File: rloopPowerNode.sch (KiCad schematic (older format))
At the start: 93 parts, among them P1 CONN_01X02, P10 CONN_01X03, P11 CONN_01X03, P13 CONN_01X03, P14 CONN_01X03, P15 CONN_01X01, P16 CONN_01X01, P17 CONN_01X08, P18 CONN_01X02, P19 CONN_01X02, P2 CONN_01X02, P20 CONN_01X02, P21 CONN_01X02, P22 AMPMODU-02X05, P23 SHUNT, P3 CONN_01X02, P4 CONN_01X02, P5 CONN_01X01, P6 CONN_01X04, P7 CONN_01X02, P8 CONN_01X02, P9 CONN_01X02, Q1 PMOS, Q2 NMOS, Q3 BSS84, U1 CPC1718, U10 AMC1100, U2 CPC1718, U3 H11F1SM, U4 MAX6814, U5 CPC1718, U6 CPC1718, U7 DS2482-100, U8 MS5607-02BA03, U9 78L05

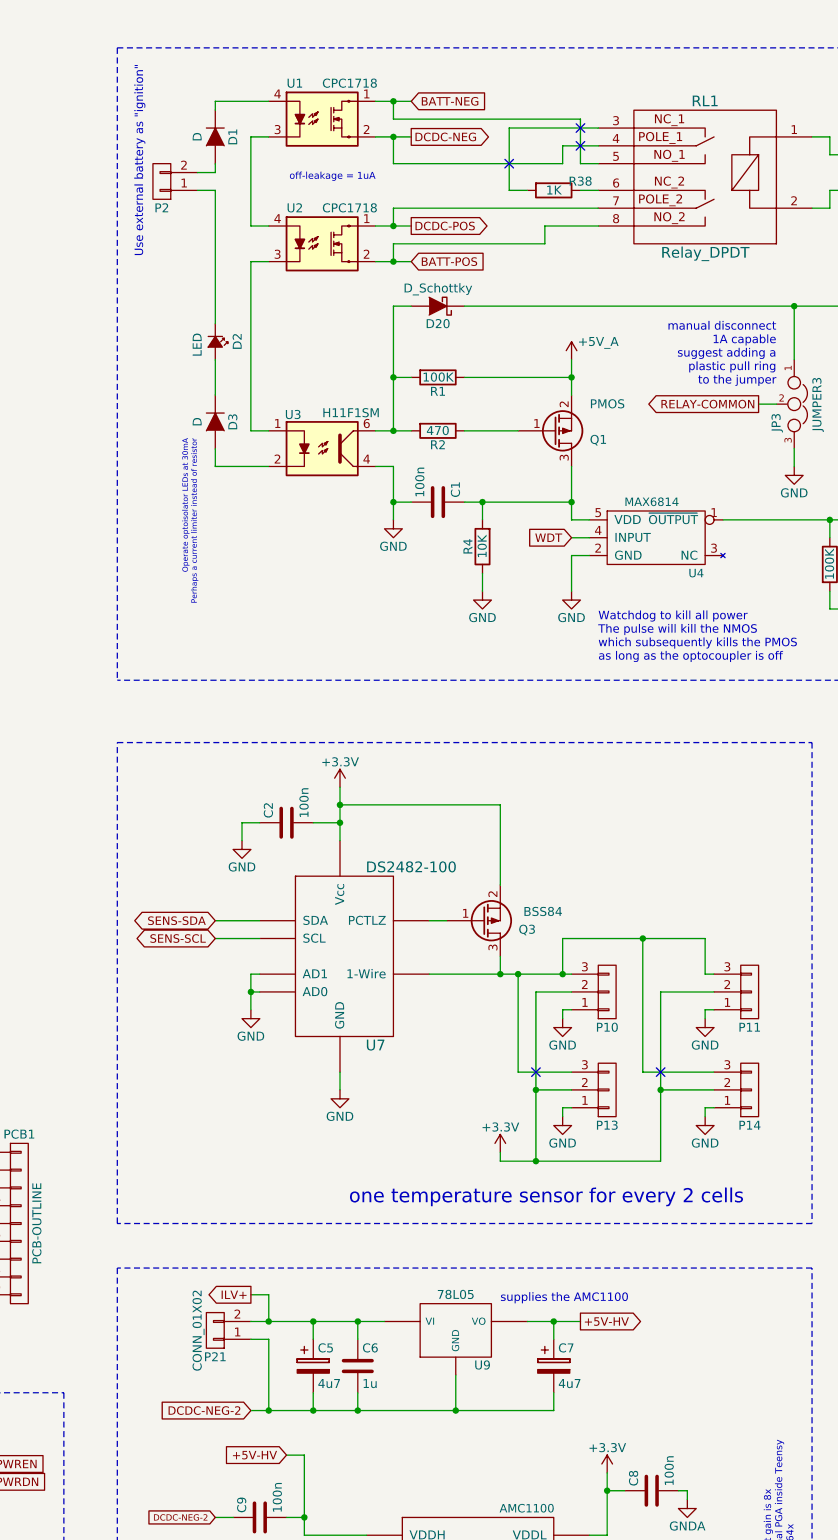
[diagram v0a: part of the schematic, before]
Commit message: added diode for 78L05, moved some stuff, more routing
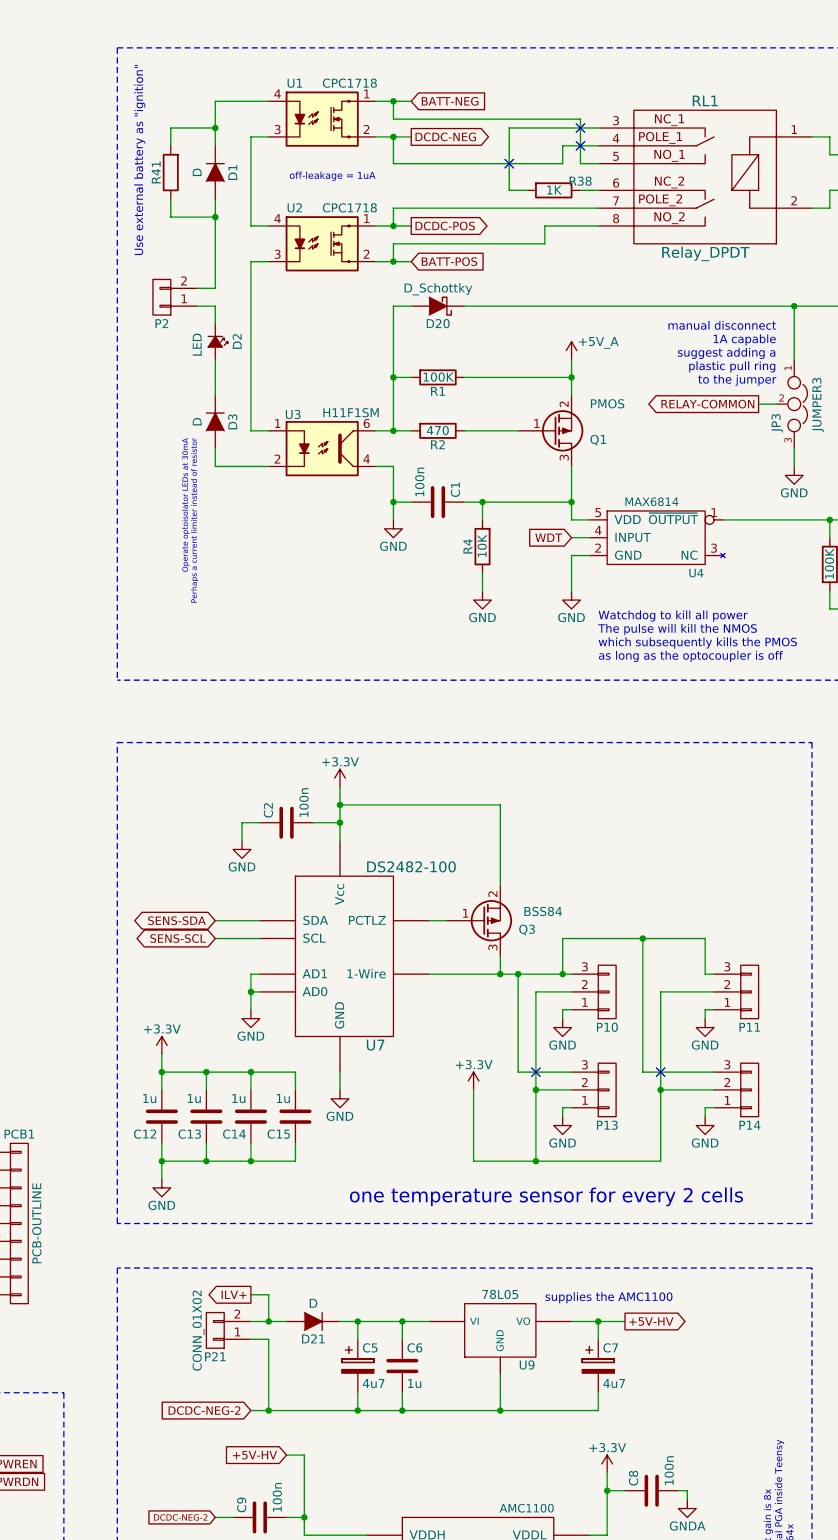
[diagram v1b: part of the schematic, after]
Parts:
- added C12, C13, C14, C15: 1u, Capacitors_SMD:C_0603, symbol C
- added D21: D, Diodes_SMD:SOD-123, symbol D
- added R41: ?, Resistors_SMD:R_0603, symbol R
- F2: footprint Resistors_ThroughHole:Resistor_Horizontal_RM15mm -> -footprints:FUSE-MULTICHOICE
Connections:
- net +3V3: now also C12.2, C13.2, C14.2, C15.2
- net GND: now also C12.1, C13.1, C14.1, C15.1
- net ILV+: now also D21.2 (A); no longer C5.1, C6.1, U9.VI
- net at D1.1 (K), U1.4: now also R41.2
- net at D1.2 (A), P2.2 (P2): now also R41.1
- new net: C5.1, C6.1, D21.1 (K), U9.VI
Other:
- moved on the sheet: C5, C6, C7, D1, P2, U9

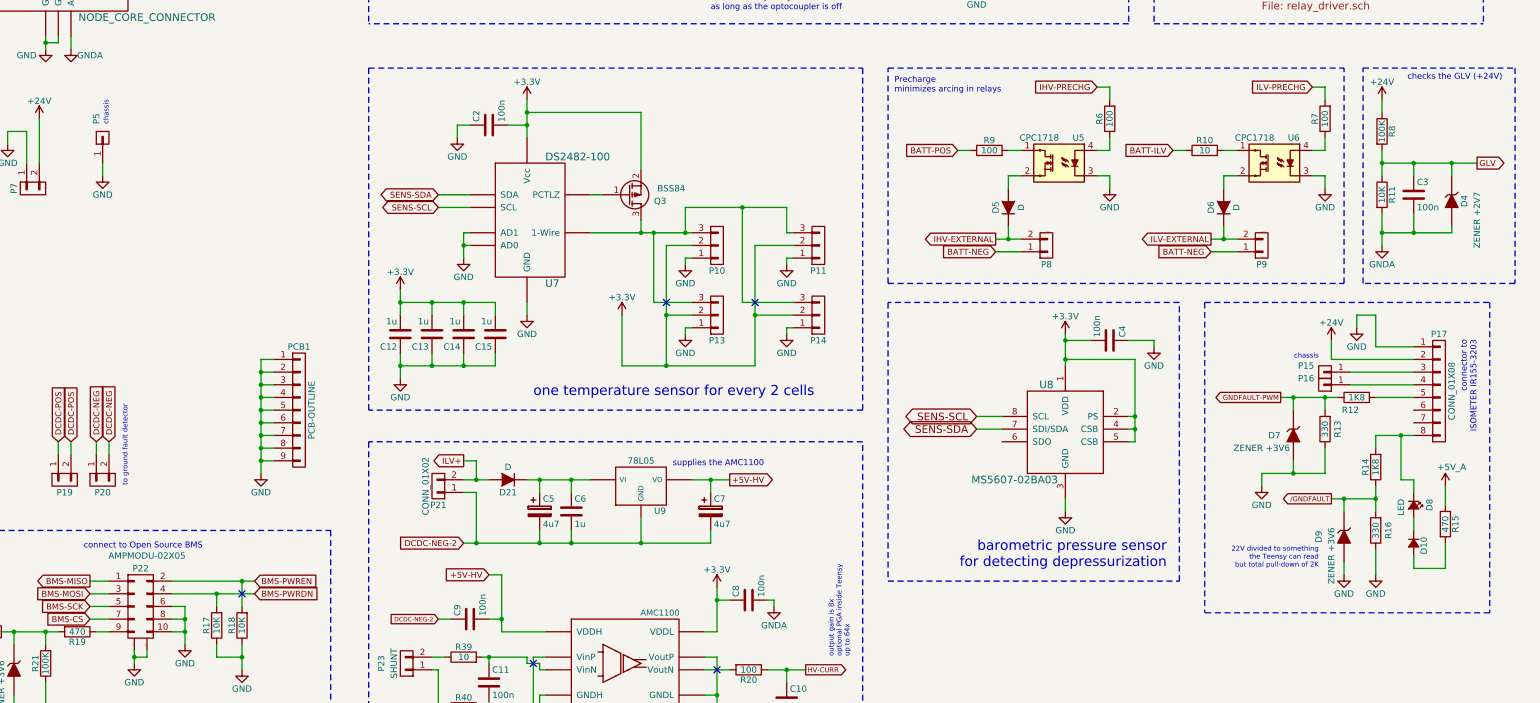
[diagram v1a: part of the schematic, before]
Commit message: got rid of isometer connector
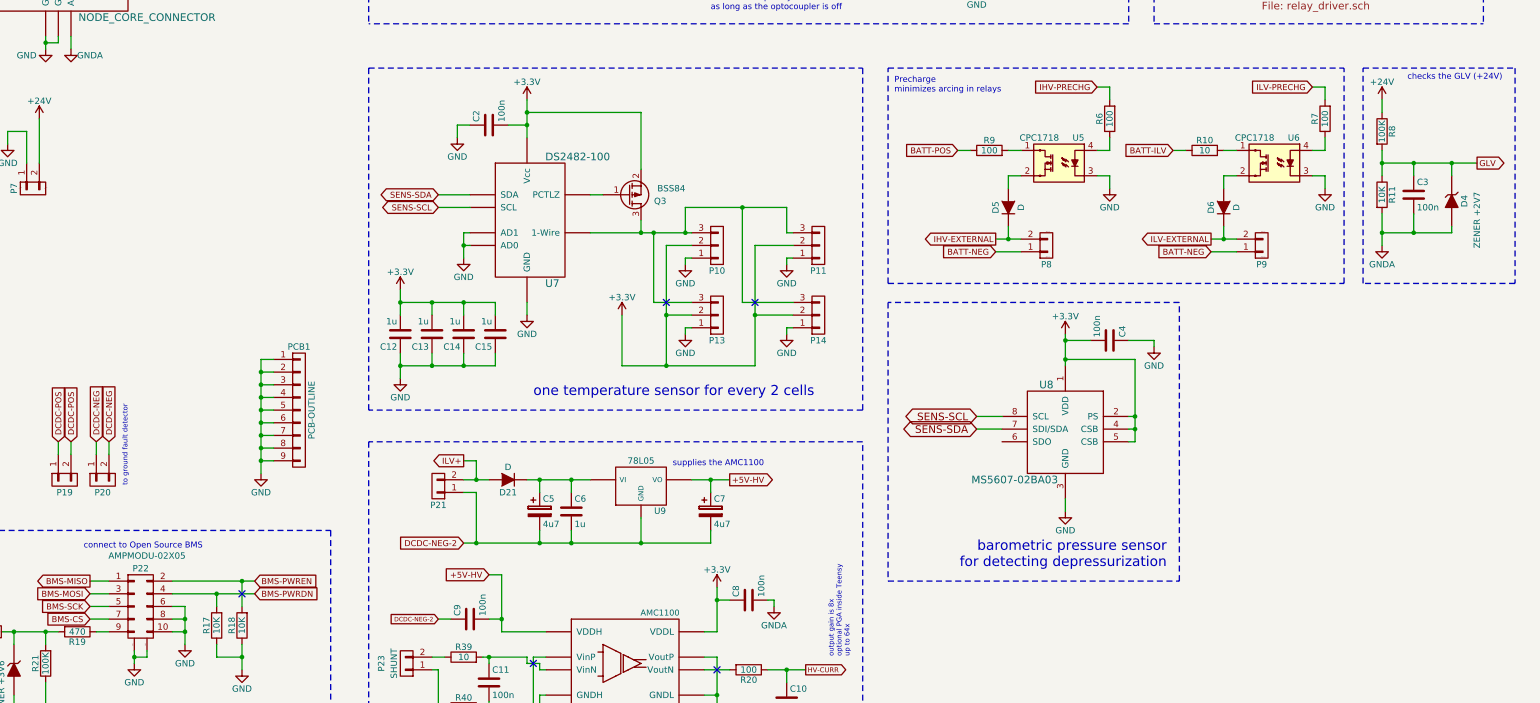
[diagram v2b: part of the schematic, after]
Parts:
- removed D10: D, Diodes_SMD:SOD-123, symbol D_Small
- removed D7, D9: ZENER +3V6, Diodes_SMD:SOD-123, symbol ZENER
- removed D8: LED, LEDs:LED_0603, symbol Led_Small
- removed P15, P16, P5: CONN_01X01, -footprints:SCREWPAD-4-40, symbol CONN_01X01
- removed P17: CONN_01X08, -footprints:CONN-JST-XH-8-PTH-RGT, symbol CONN_01X08
- removed R12, R14: 1K8, Resistors_SMD:R_1206_HandSoldering, symbol R
- removed R13, R16: 330, Resistors_SMD:R_1206_HandSoldering, symbol R
- removed R15: 470, Resistors_SMD:R_0603, symbol R
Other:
- note removed: "22V divided to something\nthe Teensy can read\nbut total pull-down of 2K"
- note removed: "chassis"
- note removed: "connector to\nISOMETER IR155-3203"

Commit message: reordered all reference designators
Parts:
- renumbered C6 to C10, C7 to C11, C8 to C12, C9 to C13, C11 to C14, C10 to C15, C12 to C4, C13 to C5, C14 to C6, C15 to C7, C4 to C8, C5 to C9, D20 to D2, D2 to D3, D3 to D4, D4 to D5, D5 to D6, D6 to D7, D21 to D8, D11 to D9, JP6 to JP4, JP4 to JP5, JP5 to JP6, P9 to P10, P13 to P11, P14 to P12, P18 to P13, P19 to P14, P20 to P15, P21 to P16, P22 to P17, P23 to P18, P6 to P5, P7 to P6, P10 to P7, P11 to P8, P8 to P9, R41 to R1, R8 to R10, R9 to R11, R10 to R12, R11 to R13, R17 to R14, R18 to R15, R19 to R16, R39 to R17, R21 to R18, R20 to R19, R38 to R2, R40 to R20, R1 to R3, R2 to R4, R3 to R5, R4 to R6, R5 to R7, R6 to R8, R7 to R9

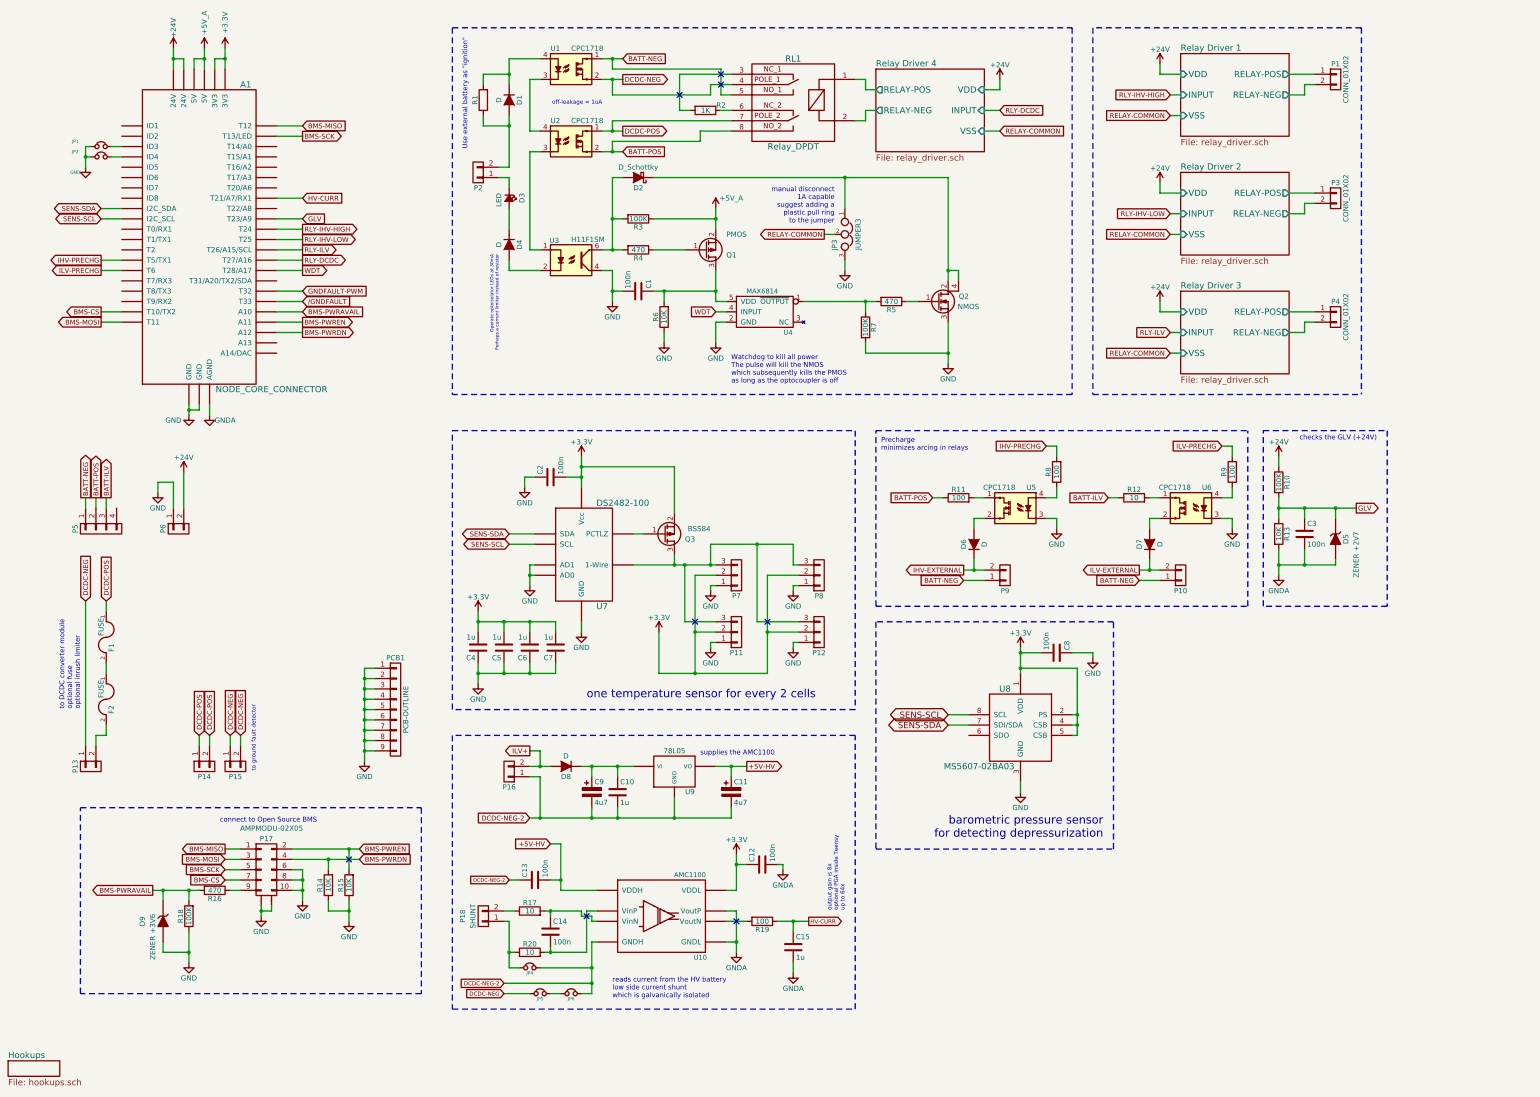
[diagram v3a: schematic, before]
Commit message: laid out BMS section
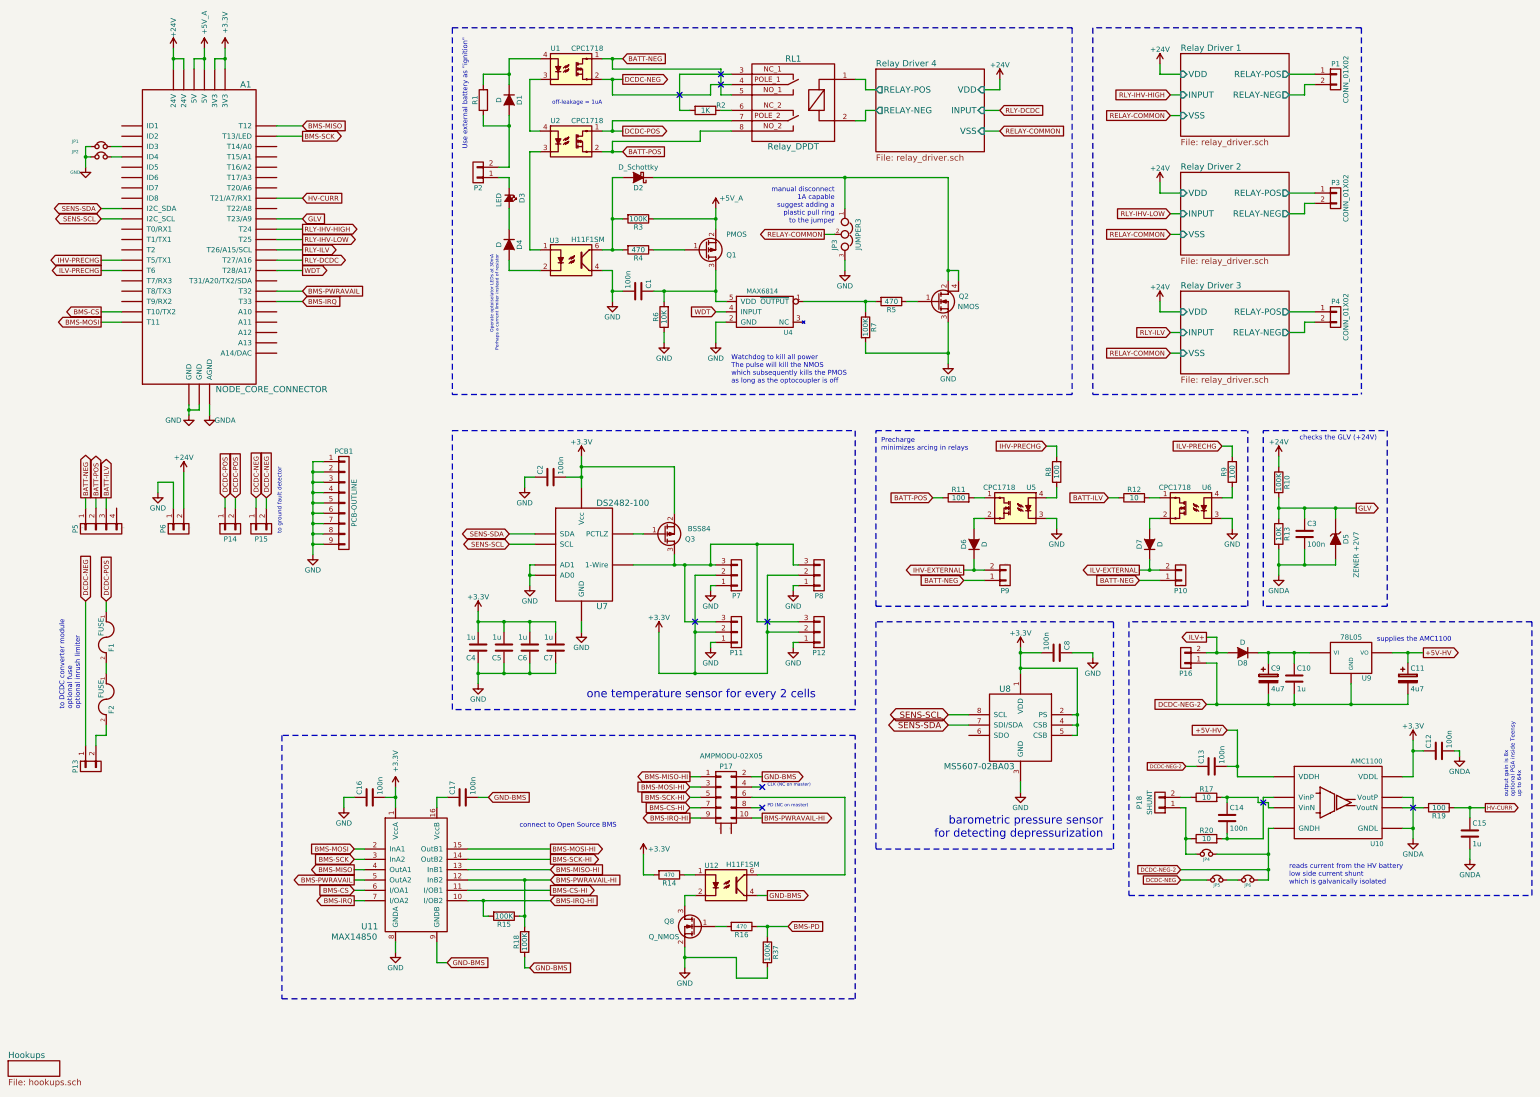
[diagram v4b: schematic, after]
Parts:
- removed D9: ZENER +3V6, Diodes_SMD:SOD-123, symbol ZENER
- added C16, C17: 100n, Capacitors_SMD:C_0603, symbol C
- added Q8: Q_NMOS, TO_SOT_Packages_SMD:SOT-23, symbol Q_NMOS_GSD
- added R37: 100K, Resistors_SMD:R_0603, symbol R
- added U11: MAX14850, Housings_SSOP:TSSOP-16_4.4x5mm_Pitch0.65mm, symbol MAX14850
- added U12: H11F1SM, -footprints:OPTOCOUPLER-0.1in-6pin-SMD, symbol OPTOISO
- P17: footprint -footprints:AMPMODU-MALE-02X05-0.05in -> -footprints:BMS
- R14: value 10K -> 470
- R15: value 10K -> 100K
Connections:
- net GNDFAULT-PWM is gone; now on net BMS-PWRAVAIL: A1.T32
- net +3V3: now also R14.2, C16.2, U11.1 (VccA)
- net BMS-CS: now also U11.6 (I/OA1); no longer P17.7 (P7)
- net BMS-MISO: now also U11.4 (OutA1); no longer P17.1 (P1)
- net BMS-MOSI: now also U11.2 (InA1); no longer P17.3 (P3)
- net BMS-PWRAVAIL: now also U11.5 (OutA2); no longer A1.A10, R16.2, R18.2
- net BMS-SCK: now also U11.3 (InA2); no longer P17.5 (P5)
- net GND: now also C16.1, Q8.2 (S), R37.2, U11.8 (GNDA); no longer P17.10 (P10), P17.6 (P6), P17.8 (P8), P17.M1, P17.M2, R14.1, R15.1, R18.1
- net BMS-IRQ-HI: now reaches P17.9 (P9)
- net BMS-IRQ-HI: now also R15.2, U11.10 (I/OB2); no longer R16.1
- net /GNDFAULT renamed BMS-IRQ
- net BMS-IRQ: now also U11.7 (I/OA2)
- removed net BMS-PWRDN: A1.A12, P17.4 (P4), R14.2
- removed net BMS-PWREN: A1.A11, P17.2 (P2), R15.2
- new net: P17.6 (P6), U12.6
- new net: C17.1, U11.16 (VccB)
- new net: R14.1, U12.1
- new net: Q8.3 (D), U12.2
- new net: Q8.1 (G), R16.2
- new net BMS-CS-HI: P17.7 (P7), U11.11 (I/OB1)
- new net BMS-MISO-HI: P17.1 (P1), U11.13 (InB1)
- new net BMS-MOSI-HI: P17.3 (P3), U11.15 (OutB1)
- new net BMS-PD: R16.1, R37.1
- new net BMS-PWRAVAIL-HI: P17.10 (P10), R15.1, R18.2, U11.12 (InB2)
- new net BMS-SCK-HI: P17.5 (P5), U11.14 (OutB2)
- new net GND-BMS: C17.2, P17.2 (P2), R18.1, U11.9 (GNDB), U12.4
- no-connect marks 8 -> 9
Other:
- note added: "CLK (NC on master)"
- note added: "PD (NC on master)"
- moved on the sheet: C10, C11, C12, C13, C14, C15, C9, D8, JP4, JP5, JP6, P14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
